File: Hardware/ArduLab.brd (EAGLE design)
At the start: 80 x 100 mm, 91 parts, among them CN1 USB-B, CN2 JST-PH, Q1 BSS138, Q2 BSS138, U1 ATMEGA32U4-AU, U2 MIC5205, U3 PAM2401, U4 MCP73831, U5 L293DD, X1 16MHz

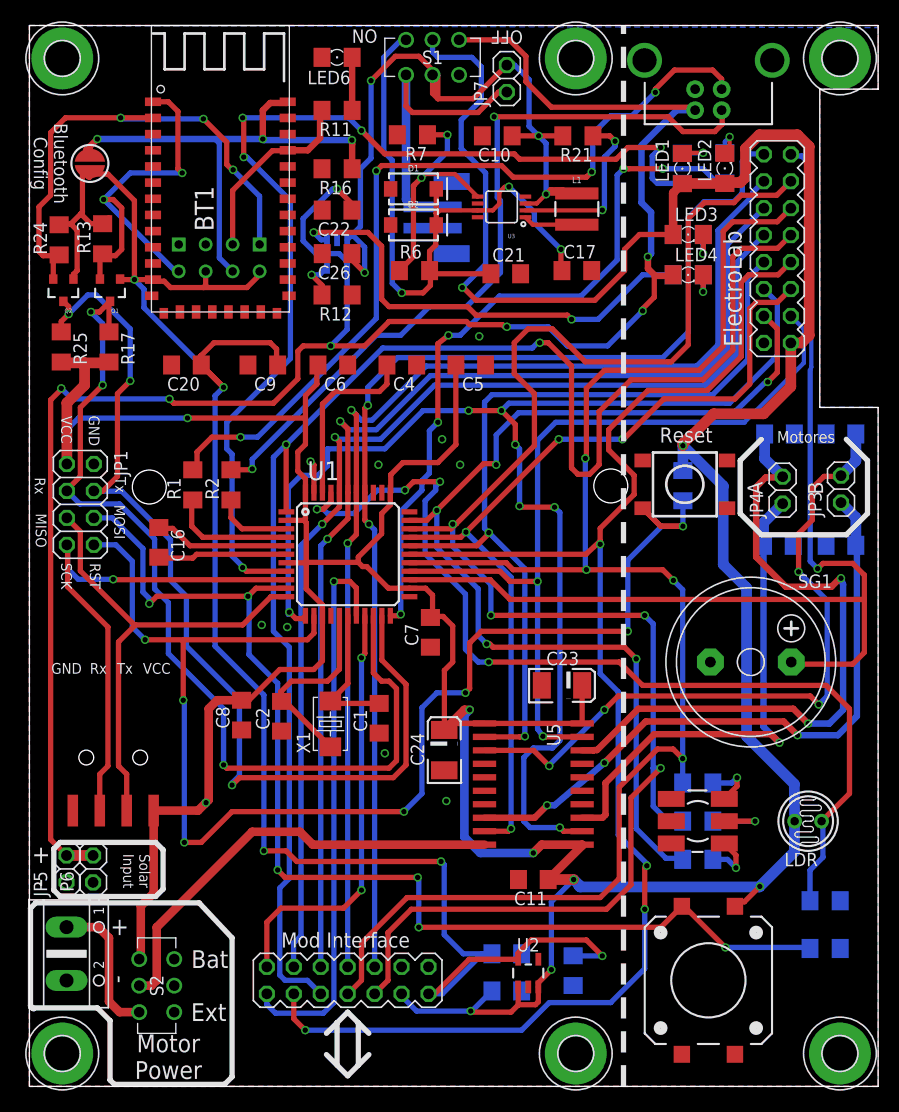
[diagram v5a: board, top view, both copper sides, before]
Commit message: Added support for Serial interface in Mod connector
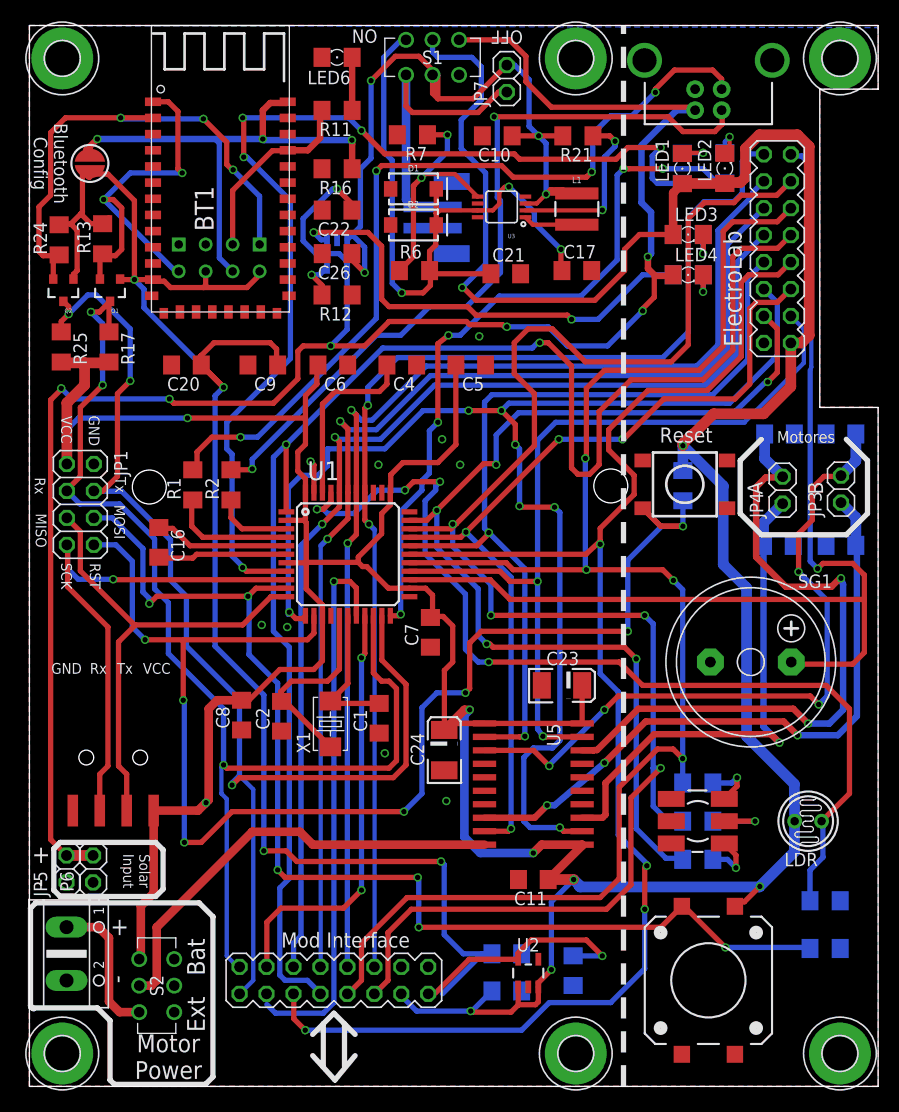
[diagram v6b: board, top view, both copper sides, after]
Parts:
- SV2: value Mods -> (none); device con-lstb:MA07-2 -> con-lstb:MA08-2
- moved SV2 1.30 mm to (28.7, 10.0)
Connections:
- net 3.3V: now also SV2.15; no longer SV2.13
- net A1: now also SV2.12; no longer SV2.10
- net A2: now also SV2.10; no longer SV2.8
- net A3: now also SV2.8; no longer SV2.6
- net A4: now also SV2.6; no longer SV2.4
- net D0: now also SV2.2
- net D1: now also SV2.1
- net D2: now also SV2.4; no longer SV2.2
- net D3: now also SV2.3; no longer SV2.1
- net D5: now also SV2.11; no longer SV2.9
- net D6: now also SV2.9; no longer SV2.7
- net D7: now also SV2.7; no longer SV2.5
- net D8: now also SV2.5; no longer SV2.3
- net GND: now also SV2.14; no longer SV2.12
- net VCC: now also SV2.13; no longer SV2.11
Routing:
- net D1: track 95.9 -> 117.5 mm
- net D0: track 89.7 -> 109.4 mm
- net 3.3V: track 181.0 -> 179.2 mm
- net D3: track 52.8 -> 51.8 mm

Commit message: Updated Mod Interface for RadioLab compatibility
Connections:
- net 3.3V: now also SV2.13; no longer SV2.15
- net GND: now also SV2.16
- net VCC: now also SV2.15; no longer SV2.13
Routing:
- net 3.3V: track 179.2 -> 181.8 mm, vias 5 -> 6
- net VCC: track 437.1 -> 434.7 mm
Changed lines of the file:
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@@
 <contactref element="R7" pad="2"/>
 <contactref element="SV2" pad="14"/>
+<contactref element="SV2" pad="16"/>
+<wire x1="35.05" y1="11.27" x2="37.59" y2="11.27" width="0" layer="19" extent="1-1"/>
 </signal>
 <signal name="AREF">
@@
 <wire x1="33.2" y1="52.1" x2="31" y2="49.9" width="0.5" layer="1"/>
 <wire x1="31" y1="49.9" x2="31" y2="49.4" width="0.5" layer="1"/>
-<wire x1="35.08" y1="8.52" x2="36.5" y2="7.1" width="0.5" layer="16"/>
-<wire x1="36.5" y1="7.1" x2="41.6" y2="7.1" width="0.5" layer="16"/>
 <wire x1="41.7" y1="7.1" x2="43.6" y2="9" width="0.5" layer="16"/>
 <wire x1="66.5" y1="16.975" x2="66.5" y2="17.4" width="0.5" layer="1"/>
@@
 <wire x1="56.1" y1="78.9" x2="57.5" y2="80.3" width="0.5" layer="1"/>
 <wire x1="57.5" y1="80.3" x2="60.678" y2="80.3" width="0.5" layer="1"/>
-<contactref element="SV2" pad="13"/>
-<wire x1="35.08" y1="8.52" x2="35.05" y2="8.73" width="0" layer="19" extent="16-16"/>
+<contactref element="SV2" pad="15"/>
+<wire x1="41.6" y1="7.1" x2="39.22" y2="7.1" width="0.4064" layer="16"/>
+<wire x1="39.22" y1="7.1" x2="37.59" y2="8.73" width="0.4064" layer="16"/>
 </signal>
 <signal name="D15">
@@
 <contactref element="C19" pad="1"/>
 <contactref element="C20" pad="1"/>
-<wire x1="38.93" y1="8.73" x2="42.7" y2="12.5" width="0.5" layer="16"/>
-<wire x1="42.7" y1="12.5" x2="43.6" y2="12.5" width="0.5" layer="16"/>
 <wire x1="46.07" y1="11.9801" x2="41.4501" y2="11.9801" width="0.5" layer="1"/>
-<wire x1="41.4501" y1="11.9801" x2="38.2" y2="8.73" width="0.5" layer="1"/>
 <wire x1="46.07" y1="11.9801" x2="46.07" y2="12.57" width="0.5" layer="1"/>
 <wire x1="46.07" y1="12.57" x2="47.3" y2="13.8" width="0.5" layer="1"/>
@@
 <wire x1="23.3" y1="69.5" x2="23.3" y2="68.1" width="0.5" layer="1"/>
 <wire x1="23.3" y1="68.1" x2="23.4" y2="68" width="0.5" layer="1"/>
-<wire x1="42.7" y1="12.5" x2="40.9" y2="12.5" width="0.5" layer="16"/>
-<wire x1="40.9" y1="12.5" x2="39.1" y2="14.3" width="0.5" layer="16"/>
+<wire x1="43.6" y1="12.5" x2="40.9" y2="12.5" width="0.5" layer="16"/>
+<wire x1="40.9" y1="12.5" x2="40.3" y2="13.1" width="0.5" layer="16"/>
+<wire x1="40.3" y1="13.1" x2="39.1" y2="14.3" width="0.5" layer="16"/>
 <wire x1="39.1" y1="14.3" x2="39.1" y2="20.9" width="0.5" layer="16"/>
 <wire x1="39.1" y1="20.9" x2="38.8" y2="21.2" width="0.5" layer="16"/>
@@
 <wire x1="3.9" y1="81.3" x2="2.878" y2="81.3" width="0.5" layer="1"/>
 <wire x1="2.878" y1="81.3" x2="2.8" y2="81.222" width="0.5" layer="1"/>
-<contactref element="SV2" pad="15"/>
-<wire x1="37.59" y1="8.73" x2="38.2" y2="8.73" width="0" layer="19" extent="1-1"/>
-<wire x1="38.93" y1="8.73" x2="38.2" y2="8.73" width="0" layer="19" extent="1-16"/>
+<contactref element="SV2" pad="13"/>
+<wire x1="41.4501" y1="11.9801" x2="41.3801" y2="11.9801" width="0.4064" layer="1"/>
+<wire x1="41.3801" y1="11.9801" x2="40.7" y2="11.3" width="0.4064" layer="1"/>
+<wire x1="40.7" y1="11.3" x2="40.7" y2="8.8" width="0.4064" layer="1"/>
+<wire x1="40.7" y1="8.8" x2="38.5" y2="6.6" width="0.4064" layer="1"/>
+<wire x1="38.5" y1="6.6" x2="35.6" y2="6.6" width="0.4064" layer="1"/>
+<wire x1="35.6" y1="6.6" x2="35.1" y2="7.1" width="0.4064" layer="1"/>
+<wire x1="35.1" y1="7.1" x2="35.1" y2="8.68" width="0.4064" layer="1"/>
+<wire x1="35.1" y1="8.68" x2="35.05" y2="8.73" width="0.4064" layer="1"/>
+<wire x1="41.3801" y1="11.9801" x2="41.3801" y2="12.0199" width="0.4064" layer="1"/>
+<wire x1="41.3801" y1="12.0199" x2="40.9" y2="12.5" width="0.4064" layer="1"/>
+<via x="40.9" y="12.5" extent="1-16" drill="0.5"/>
 </signal>
 <signal name="N$12">

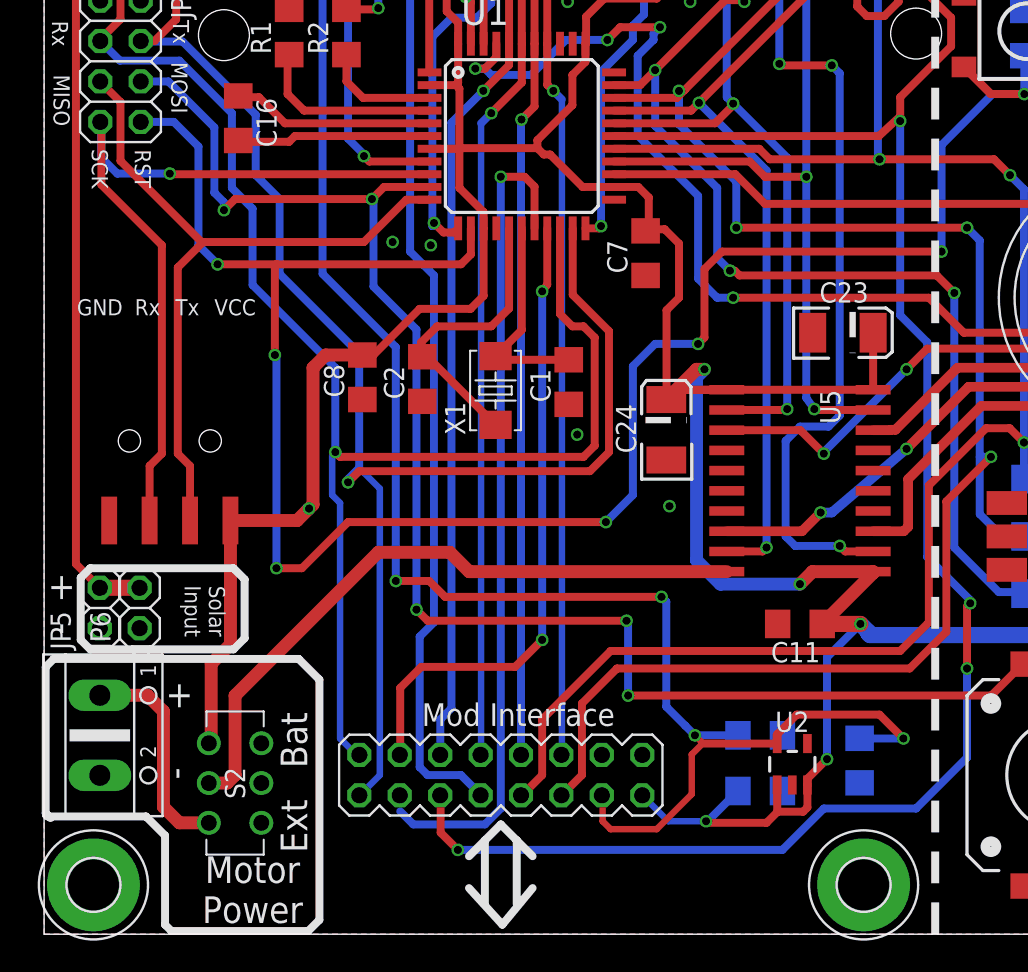
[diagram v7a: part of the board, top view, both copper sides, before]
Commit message: New Mod Interface position layout (25x6.5mm)
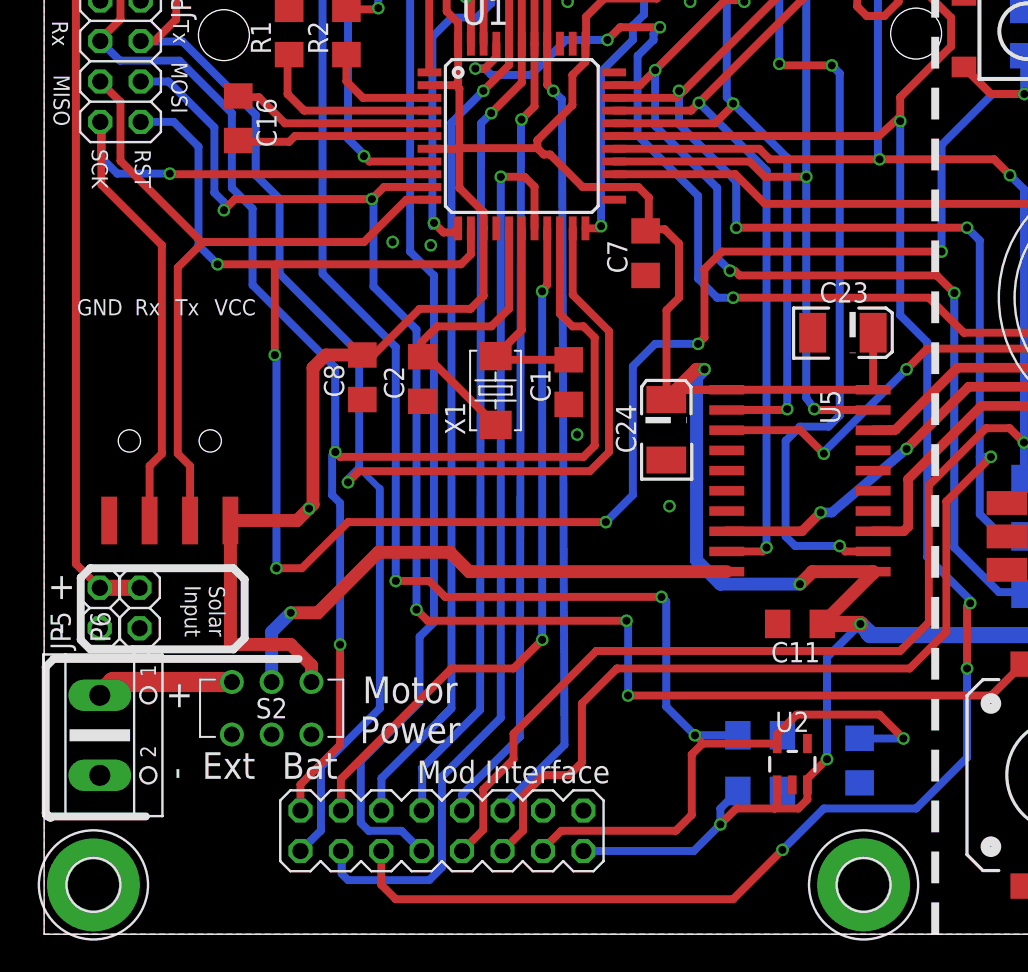
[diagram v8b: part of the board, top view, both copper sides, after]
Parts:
- moved S2 5.23 mm to (14.3, 14.2), turned to 180 degrees
- moved SV2 5.09 mm to (25.0, 6.50)
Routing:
- net V_MOT: track 42.0 -> 34.3 mm, vias 0 -> 1
- net A4: track 105.8 -> 112.5 mm
- net D3: track 51.8 -> 58.2 mm
- net D5: track 158.0 -> 164.0 mm
- net D6: track 143.4 -> 149.0 mm
- net A1: track 109.6 -> 114.8 mm
- net A3: track 107.6 -> 112.6 mm
- net D1: track 117.5 -> 122.5 mm
- net V_AUX: track 13.7 -> 8.65 mm
- net D7: track 142.2 -> 147.2 mm
- net A2: track 108.2 -> 113.2 mm
- net D8: track 139.7 -> 144.4 mm
- net D0: track 109.4 -> 113.5 mm, vias 3 -> 4
- net D2: track 40.4 -> 44.2 mm
- net 3.3V: track 181.8 -> 185.1 mm
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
